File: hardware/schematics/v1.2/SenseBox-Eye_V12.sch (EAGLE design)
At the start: 103 parts, among them IC1 ESP32-S3-WROOM-1U-N16R8, IC2 WE-CHIP_ESP32-CAM, IC3 MCP73831T-2ACI/OT, IC5 AP2127N-2.8TRG1, IC6 AP2127N-1.5TRG1, IC7 REG710NA-5, IC8 MAX17048, IC9 RP602Z330C-E2-F, J1 USB-C-S, J2 U.FL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

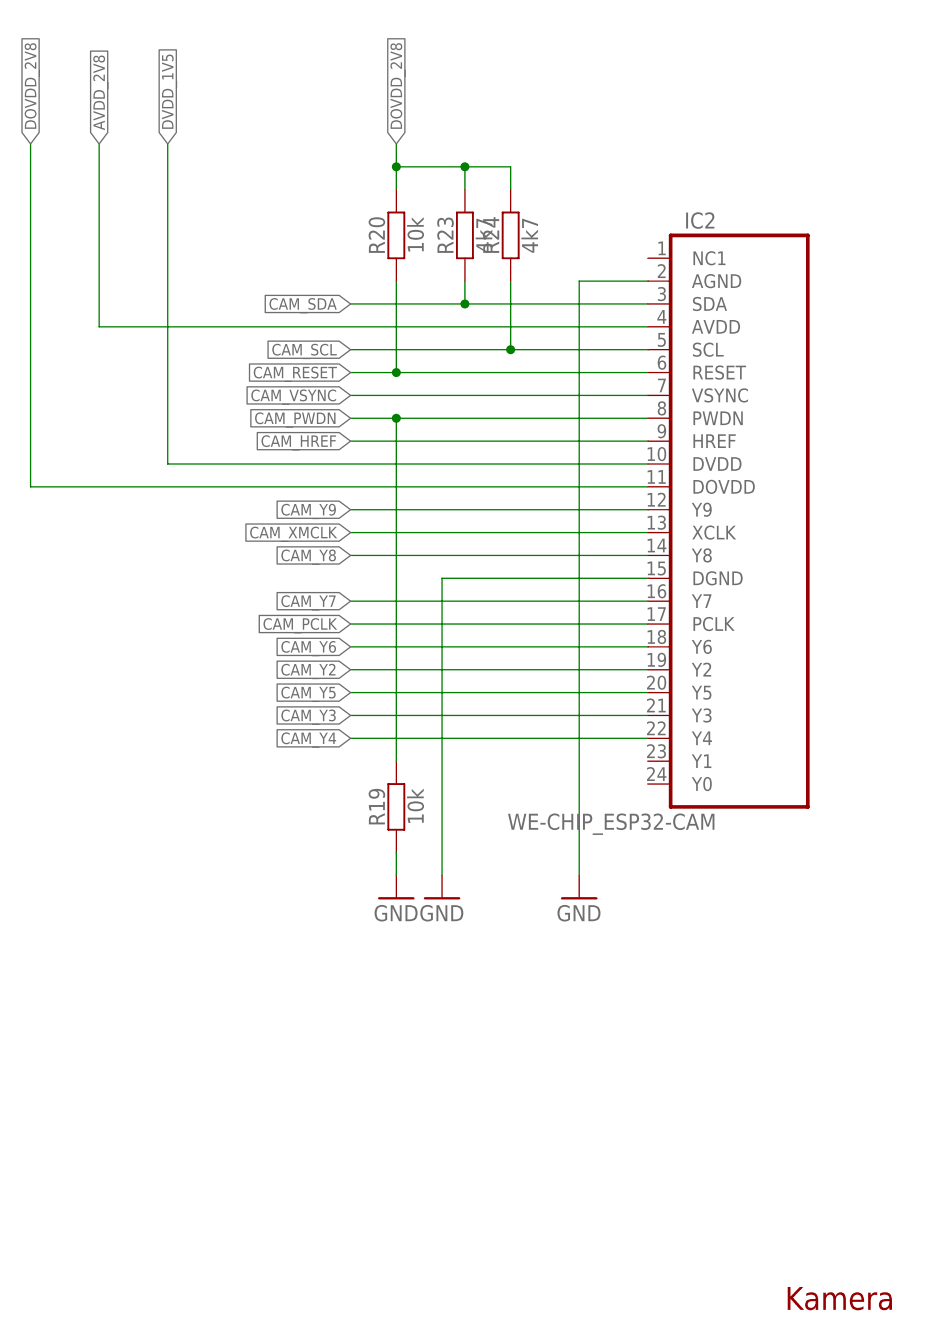
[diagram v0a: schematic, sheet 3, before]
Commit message: update v1.2 schematics
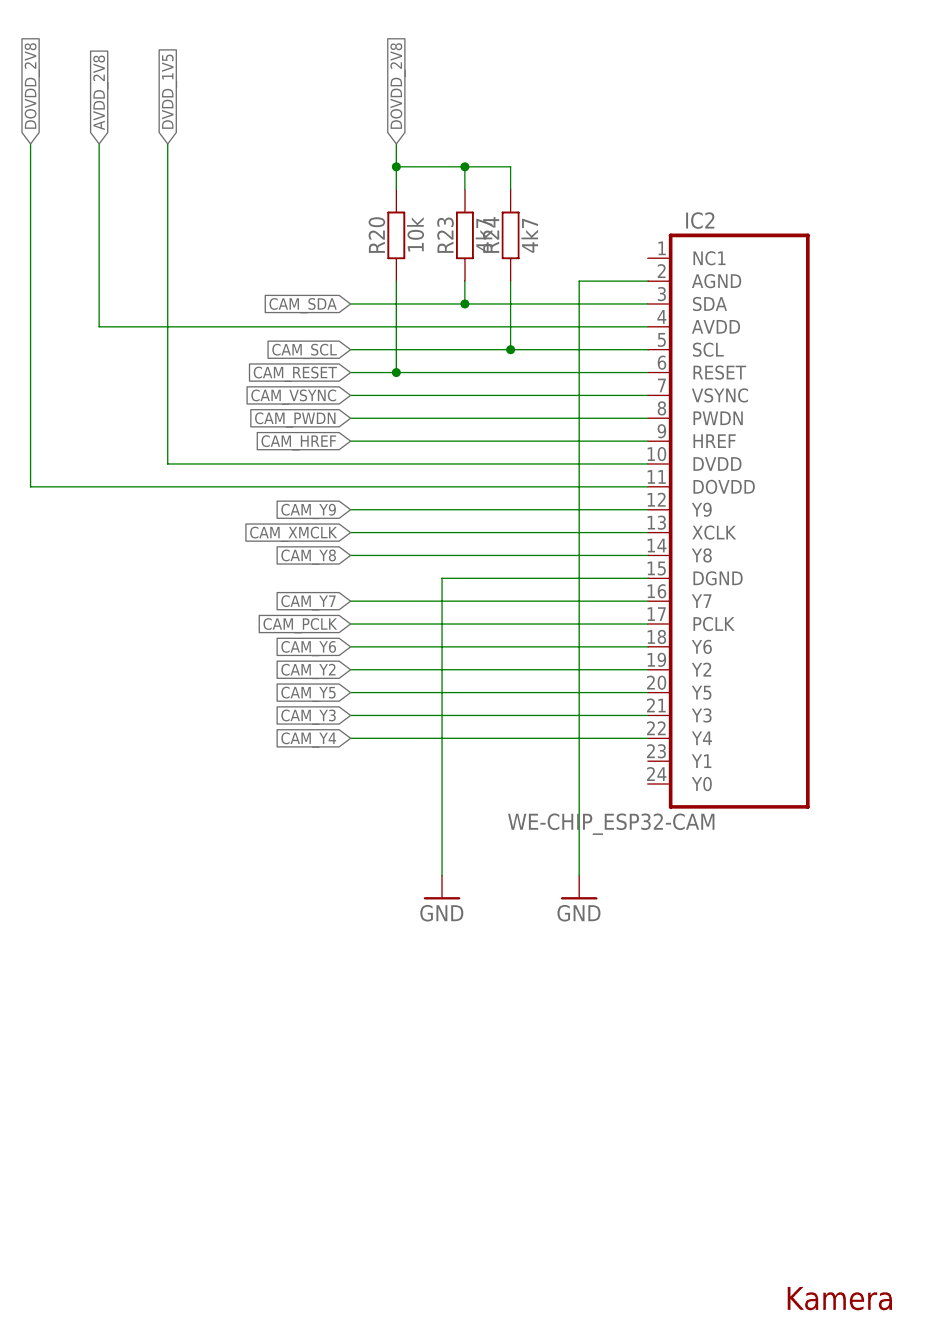
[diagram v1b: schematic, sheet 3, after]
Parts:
- removed R19: 10k, we-rcl:RESISTOR-0402
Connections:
- removed net IO46: IC1.IO46, R14.2
- net CAM_PWDN: now also IC1.IO46, R14.2; no longer R19.2
- net GND: no longer R19.1
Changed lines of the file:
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@@
 <part name="FRAME3" library="we-symbol" deviceset="FRAME-A4L" device=""/>
 <part name="FRAME4" library="we-symbol" deviceset="FRAME-A4L" device=""/>
-<part name="R19" library="we-rcl" deviceset="RESISTOR" device="-0402" value="10k"/>
 <part name="R20" library="we-rcl" deviceset="RESISTOR" device="-0402" value="10k"/>
 <part name="R2" library="we-rcl" deviceset="RESISTOR" device="-0402" value="0"/>
@@
 <part name="GND47" library="we_supply1" deviceset="GND" device=""/>
 <part name="GND48" library="we_supply1" deviceset="GND" device=""/>
-<part name="GND49" library="we_supply1" deviceset="GND" device=""/>
 <part name="GND50" library="we_supply1" deviceset="GND" device=""/>
 <part name="GND51" library="we_supply1" deviceset="GND" device=""/>
@@
 </segment>
 </net>
-<net name="IO46" class="0">
+<net name="CAM_PWDN" class="0">
 <segment>
 <pinref part="IC1" gate="G$1" pin="IO46"/>
@@
 <attribute name="SHEET" x="230.505" y="5.08" size="2.54" layer="94" font="vector" ratio="10"/>
 </instance>
-<instance part="R19" gate="R" x="119.38" y="60.96" smashed="yes" rot="R90">
-<attribute name="NAME" x="118.11" y="60.96" size="1.778" layer="95" rot="R90" align="bottom-center"/>
-<attribute name="VALUE" x="120.65" y="60.96" size="1.778" layer="96" rot="R90" align="top-center"/>
-</instance>
 <instance part="R20" gate="R" x="119.38" y="124.46" smashed="yes" rot="R90">
 <attribute name="NAME" x="118.11" y="124.46" size="1.778" layer="95" rot="R90" align="bottom-center"/>
@@
 <attribute name="NAME" x="130.81" y="124.46" size="1.778" layer="95" rot="R90" align="bottom-center"/>
 <attribute name="VALUE" x="133.35" y="124.46" size="1.778" layer="96" rot="R90" align="top-center"/>
-</instance>
-<instance part="GND49" gate="1" x="119.38" y="50.8" smashed="yes">
-<attribute name="VALUE" x="116.84" y="48.26" size="1.778" layer="96"/>
 </instance>
 <instance part="GND50" gate="1" x="124.46" y="50.8" smashed="yes">
@@
 <net name="CAM_PWDN" class="0">
 <segment>
-<wire x1="147.32" y1="104.14" x2="119.38" y2="104.14" width="0.1524" layer="91"/>
+<wire x1="147.32" y1="104.14" x2="114.3" y2="104.14" width="0.1524" layer="91"/>
 <label x="114.3" y="104.14" size="1.27" layer="95" rot="R180" xref="yes"/>
-<pinref part="R19" gate="R" pin="2"/>
-<wire x1="119.38" y1="104.14" x2="114.3" y2="104.14" width="0.1524" layer="91"/>
-<wire x1="119.38" y1="66.04" x2="119.38" y2="104.14" width="0.1524" layer="91"/>
-<junction x="119.38" y="104.14"/>
 <pinref part="IC2" gate="G$1" pin="PWDN"/>
 </segment>
@@
 </segment>
 <segment>
-<pinref part="R19" gate="R" pin="1"/>
-<wire x1="119.38" y1="53.34" x2="119.38" y2="55.88" width="0.1524" layer="91"/>
-<pinref part="GND49" gate="1" pin="GND"/>
-</segment>
-<segment>
